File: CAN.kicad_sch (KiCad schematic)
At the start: 3 parts

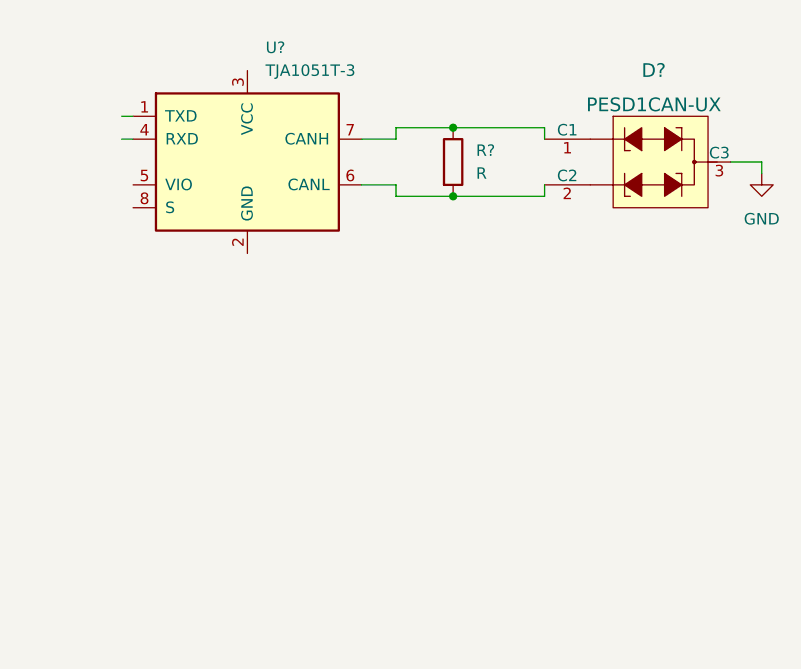
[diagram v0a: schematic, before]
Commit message: Added CAN x2
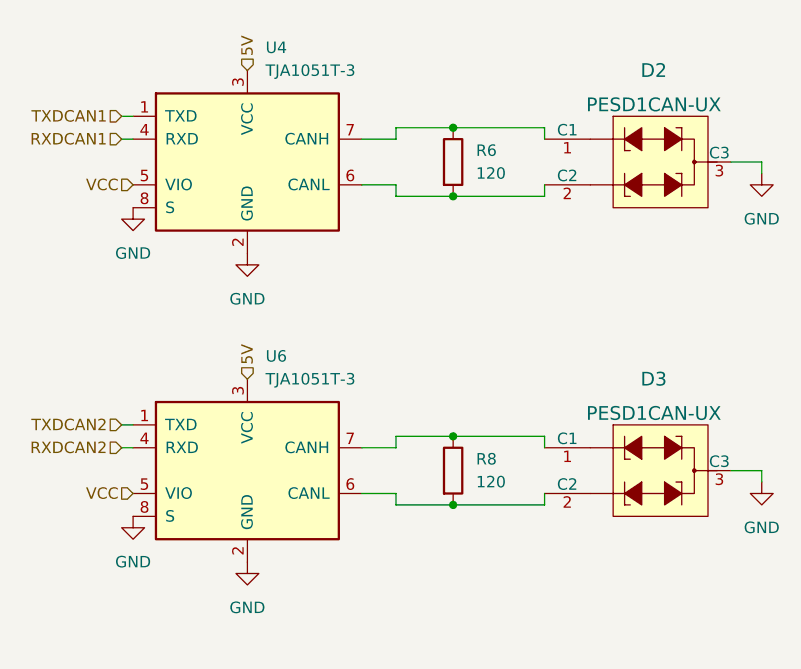
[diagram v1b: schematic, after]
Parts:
- added D3: PESD1CAN-UX, digikey-footprints:SOT-323, symbol rusefi_pesd1can:PESD1CAN-UX
- added R8: 120, Resistor_SMD:R_0402_1005Metric, symbol Device:R
- added U6: TJA1051T-3, Package_SO:SOIC-8_3.9x4.9mm_P1.27mm, symbol Interface_CAN_LIN:TJA1051T-3
- R6: renamed from R?; value R -> 120; footprint (none) -> Resistor_SMD:R_0402_1005Metric
- gave numbers to parts that had none: 2
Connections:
- net GND: now also U4.2 (GND), U4.8 (S), D3.3 (C3), U6.2 (GND), U6.8 (S)
- net TXDCAN1: now reaches U4.1 (TXD)
- net 5V: now reaches U4.3 (VCC)
- net 5V: now also U6.3 (VCC)
- net RXDCAN1: now reaches U4.4 (RXD)
- net VCC: now reaches U4.5 (VIO)
- net VCC: now also U6.5 (VIO)
- new net: D3.1 (C1), R8.1, U6.7 (CANH)
- new net: D3.2 (C2), R8.2, U6.6 (CANL)
- new net RXDCAN2: U6.4 (RXD)
- new net TXDCAN2: U6.1 (TXD)

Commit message: Converted to 4 layer
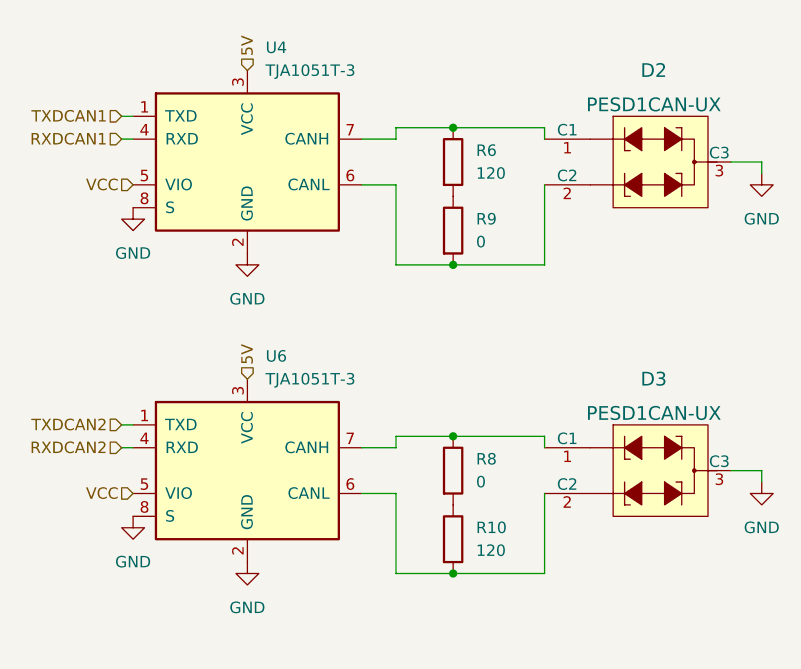
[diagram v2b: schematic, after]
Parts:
- added R10: 120, Resistor_SMD:R_0805_2012Metric, symbol Device:R
- added R9: 0, Resistor_SMD:R_0402_1005Metric, symbol Device:R
- R6: footprint Resistor_SMD:R_0402_1005Metric -> Resistor_SMD:R_0805_2012Metric
- R8: value 120 -> 0
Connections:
- net at D2.2 (C2), U4.6 (CANL): now also R9.2; no longer R6.2
- net at D3.2 (C2), U6.6 (CANL): now also R10.2; no longer R8.2
- new net: R10.1, R8.2
- new net: R6.2, R9.1
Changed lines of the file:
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@@
 (kicad_sch (version 20211123) (generator eeschema)
   (paper "A4")
-  (junction (at 132.08 134.62) (diameter 0) (color 0 0 0 0)
+  (junction (at 132.08 142.24) (diameter 0) (color 0 0 0 0)
+  )
+  (junction (at 132.08 107.95) (diameter 0) (color 0 0 0 0)
   )
   (junction (at 132.08 92.71) (diameter 0) (color 0 0 0 0)
   )
-  (junction (at 132.08 100.33) (diameter 0) (color 0 0 0 0)
-  )
   (junction (at 132.08 127) (diameter 0) (color 0 0 0 0)
   )
@@
     (stroke (width 0) (type default) (color 0 0 0 0))
   )
+  (wire (pts (xy 142.24 142.24) (xy 132.08 142.24))
+    (stroke (width 0) (type default) (color 0 0 0 0))
+  )
   (wire (pts (xy 121.92 133.35) (xy 125.73 133.35))
     (stroke (width 0) (type default) (color 0 0 0 0))
@@
     (stroke (width 0) (type default) (color 0 0 0 0))
   )
-  (wire (pts (xy 142.24 100.33) (xy 142.24 99.06))
+  (wire (pts (xy 142.24 99.06) (xy 142.24 107.95))
     (stroke (width 0) (type default) (color 0 0 0 0))
   )
@@
     (stroke (width 0) (type default) (color 0 0 0 0))
   )
-  (wire (pts (xy 125.73 100.33) (xy 132.08 100.33))
-    (stroke (width 0) (type default) (color 0 0 0 0))
-  )
-  (wire (pts (xy 132.08 100.33) (xy 142.24 100.33))
+  (wire (pts (xy 125.73 142.24) (xy 132.08 142.24))
     (stroke (width 0) (type default) (color 0 0 0 0))
   )
@@
     (stroke (width 0) (type default) (color 0 0 0 0))
   )
-  (wire (pts (xy 142.24 134.62) (xy 142.24 133.35))
+  (wire (pts (xy 142.24 133.35) (xy 142.24 142.24))
     (stroke (width 0) (type default) (color 0 0 0 0))
   )
@@
     (stroke (width 0) (type default) (color 0 0 0 0))
   )
+  (wire (pts (xy 125.73 107.95) (xy 132.08 107.95))
+    (stroke (width 0) (type default) (color 0 0 0 0))
+  )
   (wire (pts (xy 95.25 125.73) (xy 96.52 125.73))
     (stroke (width 0) (type default) (color 0 0 0 0))
   )
-  (wire (pts (xy 125.73 134.62) (xy 132.08 134.62))
+  (wire (pts (xy 142.24 107.95) (xy 132.08 107.95))
     (stroke (width 0) (type default) (color 0 0 0 0))
   )
@@
     (stroke (width 0) (type default) (color 0 0 0 0))
   )
-  (wire (pts (xy 125.73 133.35) (xy 125.73 134.62))
-    (stroke (width 0) (type default) (color 0 0 0 0))
-  )
-  (wire (pts (xy 125.73 99.06) (xy 125.73 100.33))
+  (wire (pts (xy 125.73 133.35) (xy 125.73 142.24))
+    (stroke (width 0) (type default) (color 0 0 0 0))
+  )
+  (wire (pts (xy 125.73 99.06) (xy 125.73 107.95))
     (stroke (width 0) (type default) (color 0 0 0 0))
   )
   (wire (pts (xy 125.73 92.71) (xy 132.08 92.71))
-    (stroke (width 0) (type default) (color 0 0 0 0))
-  )
-  (wire (pts (xy 132.08 134.62) (xy 142.24 134.62))
     (stroke (width 0) (type default) (color 0 0 0 0))
   )
@@
       (effects (font (size 1.27 1.27)) (justify left))
     )
-    (property "Value" "120" (id 1) (at 134.62 132.0799 0)
+    (property "Value" "0" (id 1) (at 134.62 132.0799 0)
       (effects (font (size 1.27 1.27)) (justify left))
     )
@@
       (effects (font (size 1.27 1.27)) (justify left))
     )
-    (property "Footprint" "Resistor_SMD:R_0402_1005Metric" (id 2) (at 130.302 96.52 90)
+    (property "Footprint" "Resistor_SMD:R_0805_2012Metric" (id 2) (at 130.302 96.52 90)
       (effects (font (size 1.27 1.27)) hide)
     )
@@
     (pin "1")
   )
+  (symbol (lib_id "Device:R") (at 132.08 138.43 0) (unit 1)
+    (in_bom yes) (on_board yes) (fields_autoplaced)
+    (property "Reference" "R10" (id 0) (at 134.62 137.1599 0)
+      (effects (font (size 1.27 1.27)) (justify left))
+    )
+    (property "Value" "120" (id 1) (at 134.62 139.6999 0)
+      (effects (font (size 1.27 1.27)) (justify left))
+    )
+    (property "Footprint" "Resistor_SMD:R_0805_2012Metric" (id 2) (at 130.302 138.43 90)
+      (effects (font (size 1.27 1.27)) hide)
+    )
+    (property "Datasheet" "~" (id 3) (at 132.08 138.43 0)
+      (effects (font (size 1.27 1.27)) hide)
+    )
+    (pin "1")
+    (pin "2")
+  )
+  (symbol (lib_id "Device:R") (at 132.08 104.14 0) (unit 1)
+    (in_bom yes) (on_board yes) (fields_autoplaced)
+    (property "Reference" "R9" (id 0) (at 134.62 102.8699 0)
+      (effects (font (size 1.27 1.27)) (justify left))
+    )
+    (property "Value" "0" (id 1) (at 134.62 105.4099 0)
+      (effects (font (size 1.27 1.27)) (justify left))
+    )
+    (property "Footprint" "Resistor_SMD:R_0402_1005Metric" (id 2) (at 130.302 104.14 90)
+      (effects (font (size 1.27 1.27)) hide)
+    )
+    (property "Datasheet" "~" (id 3) (at 132.08 104.14 0)
+      (effects (font (size 1.27 1.27)) hide)
+    )
+    (pin "1")
+    (pin "2")
+  )
   (symbol (lib_id "power:GND") (at 109.22 106.68 0) (unit 1)

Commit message: Fixed CAN and 5v pads
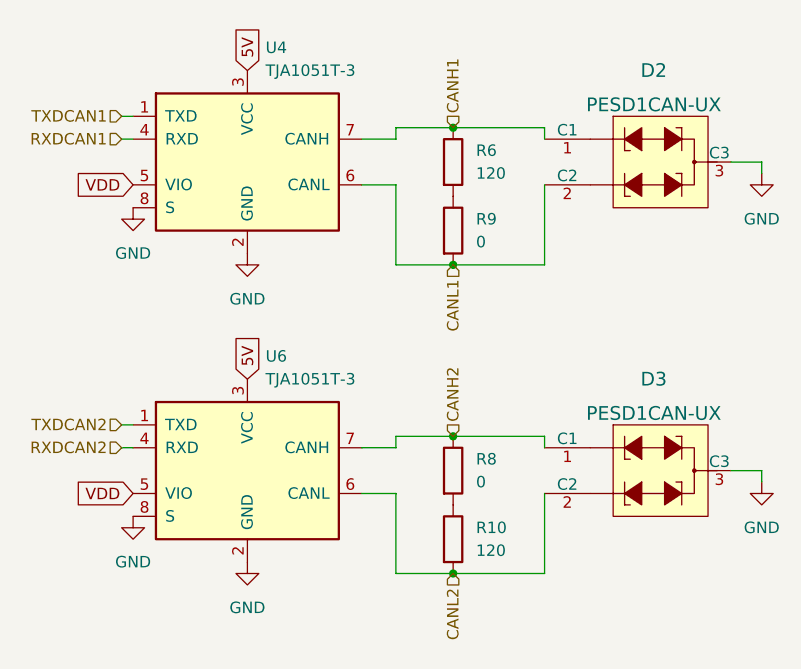
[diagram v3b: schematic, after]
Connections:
- net CANH1: now reaches D2.1 (C1), R6.1, U4.7 (CANH)
- net CANL1: now reaches D2.2 (C2), R9.2, U4.6 (CANL)
- net CANH2: now reaches D3.1 (C1), R8.1, U6.7 (CANH)
- net CANL2: now reaches D3.2 (C2), R10.2, U6.6 (CANL)
- net VCC renamed VDD
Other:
- company: (none) -> rusEFI.com
- title: (none) -> MRE IO Expander
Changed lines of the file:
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@@
 (kicad_sch (version 20211123) (generator eeschema)
   (paper "A4")
+  (title_block
+    (title "MRE IO Expander")
+    (date "2021-02-")
+    (rev "R0.1")
+    (company "rusEFI.com")
+    (comment 1 "Simon Orchard")
+  )
   (junction (at 132.08 142.24) (diameter 0) (color 0 0 0 0)
   )
@@
     (stroke (width 0) (type default) (color 0 0 0 0))
   )
+  (global_label "5V" (shape input) (at 109.22 120.65 90) (fields_autoplaced)
+    (effects (font (size 1.27 1.27)) (justify left))
+    (property "Intersheet References" "${INTERSHEET_REFS}" (id 0) (at 109.1406 116.0277 90)
+      (effects (font (size 1.27 1.27)) (justify left) hide)
+    )
+  )
+  (global_label "VDD" (shape input) (at 96.52 133.35 180) (fields_autoplaced)
+    (effects (font (size 1.27 1.27)) (justify right))
+    (property "Intersheet References" "${INTERSHEET_REFS}" (id 0) (at 90.5672 133.2706 0)
+      (effects (font (size 1.27 1.27)) (justify right) hide)
+    )
+  )
+  (global_label "VDD" (shape input) (at 96.52 99.06 180) (fields_autoplaced)
+    (effects (font (size 1.27 1.27)) (justify right))
+    (property "Intersheet References" "${INTERSHEET_REFS}" (id 0) (at 90.5672 98.9806 0)
+      (effects (font (size 1.27 1.27)) (justify right) hide)
+    )
+  )
+  (global_label "5V" (shape input) (at 109.22 86.36 90) (fields_autoplaced)
+    (effects (font (size 1.27 1.27)) (justify left))
+    (property "Intersheet References" "${INTERSHEET_REFS}" (id 0) (at 109.1406 81.7377 90)
+      (effects (font (size 1.27 1.27)) (justify left) hide)
+    )
+  )
+  (hierarchical_label "CANL2" (shape input) (at 132.08 142.24 270)
+    (effects (font (size 1.27 1.27)) (justify right))
+  )
   (hierarchical_label "RXDCAN1" (shape input) (at 95.25 93.98 180)
     (effects (font (size 1.27 1.27)) (justify right))
   )
-  (hierarchical_label "VCC" (shape input) (at 96.52 99.06 180)
-    (effects (font (size 1.27 1.27)) (justify right))
-  )
-  (hierarchical_label "VCC" (shape input) (at 96.52 133.35 180)
-    (effects (font (size 1.27 1.27)) (justify right))
-  )
-  (hierarchical_label "5V" (shape input) (at 109.22 120.65 90)
+  (hierarchical_label "CANH1" (shape input) (at 132.08 92.71 90)
     (effects (font (size 1.27 1.27)) (justify left))
   )
@@
     (effects (font (size 1.27 1.27)) (justify right))
   )
-  (hierarchical_label "5V" (shape input) (at 109.22 86.36 90)
+  (hierarchical_label "CANH2" (shape input) (at 132.08 127 90)
     (effects (font (size 1.27 1.27)) (justify left))
   )
@@
     (effects (font (size 1.27 1.27)) (justify right))
   )
+  (hierarchical_label "CANL1" (shape input) (at 132.08 107.95 270)
+    (effects (font (size 1.27 1.27)) (justify right))
+  )
